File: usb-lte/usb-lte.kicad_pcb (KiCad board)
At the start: 4 copper layers, 26 x 45 mm, 89 parts, among them J1 Sim slot, J2 Conn_Coaxial, J3 Conn_Coaxial, J4 Conn_Coaxial, P1 USB_C_Plug_USB2.0, Q1 MBT3904DW1, Q2 MBT3904DW1, Q3 MBT3904DW1, SW1 B3U-1000P, U1 TPS62A02APDDC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

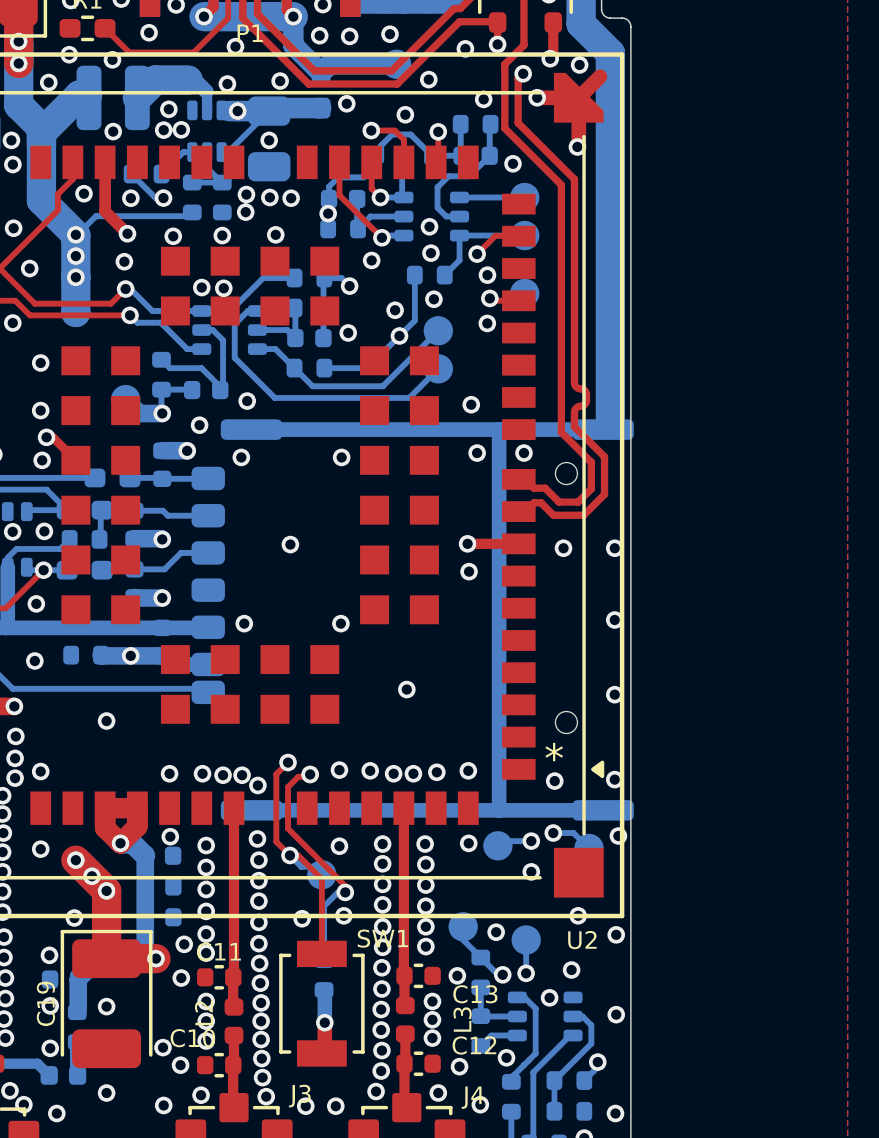
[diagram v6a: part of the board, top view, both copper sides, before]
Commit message: Update test points
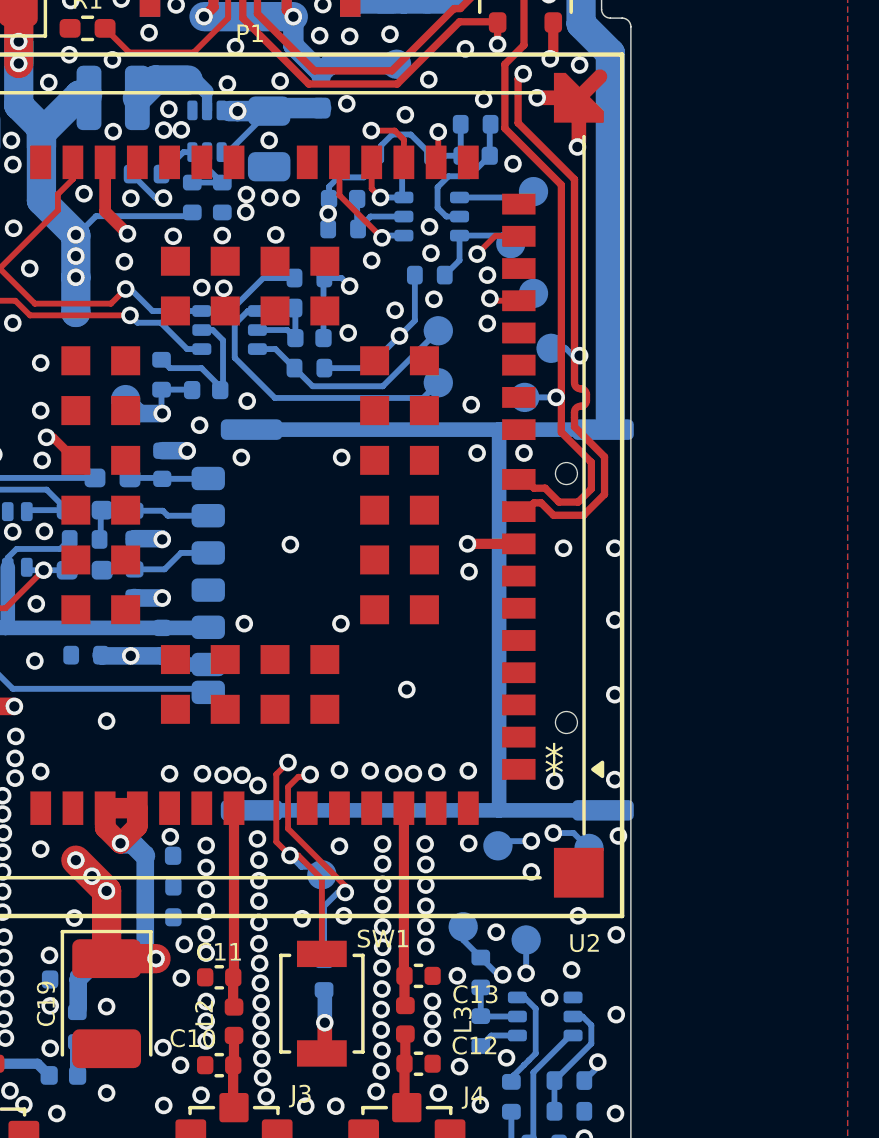
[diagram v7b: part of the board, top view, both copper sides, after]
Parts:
- added TP18: TestPoint, footprints:TestPoint_Pad_1mm, B.Cu at (160.9, 103.7)
- added TP19: TestPoint, footprints:TestPoint_Pad_1mm, B.Cu at (160.0, 105.3)
- R13: value 510k -> 560k
- moved TP10 0.55 mm to (159.5, 100.1)
- moved TP6 0.47 mm to (157.0, 104.8)
- moved TP11 0.36 mm to (160.3, 98.3)
- moved TP7 0.30 mm to (160.3, 101.8)
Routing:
- net USB_DP: track 33.5 -> 34.7 mm, vias 2 -> 3
- net USB_DN: track 34.5 -> 35.8 mm, vias 0 -> 1
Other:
- board text added: "D+"
- board text added: "D-"

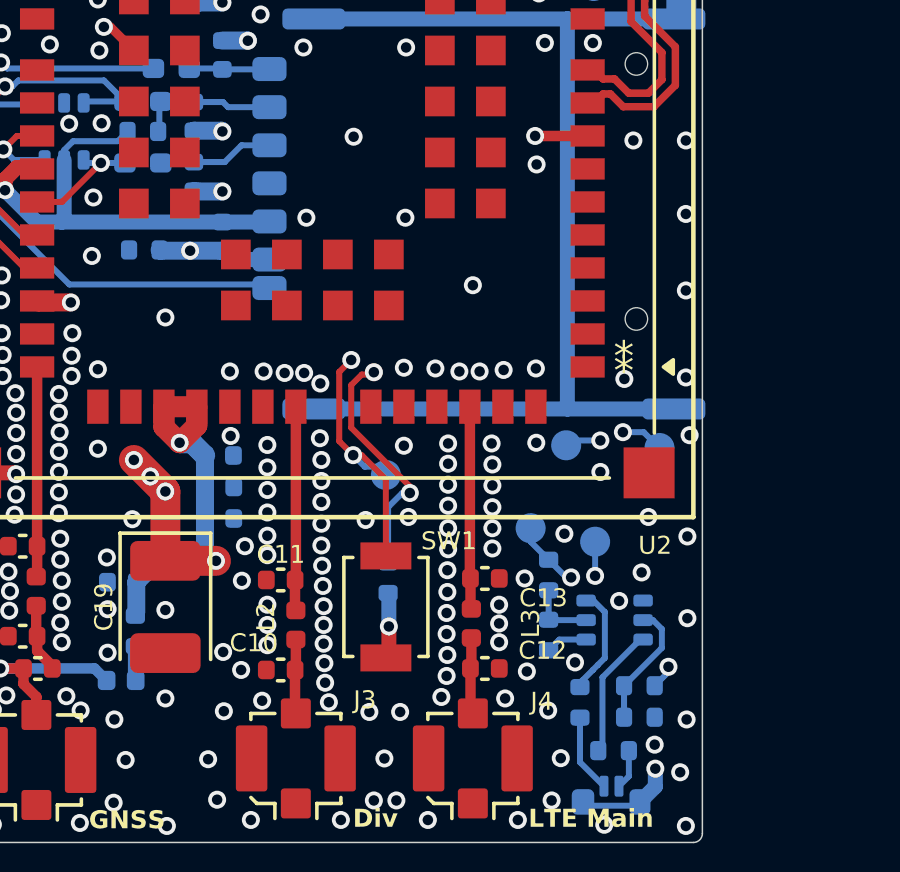
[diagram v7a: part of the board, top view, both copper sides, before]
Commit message: Remove USB boot key, add autostart pull down
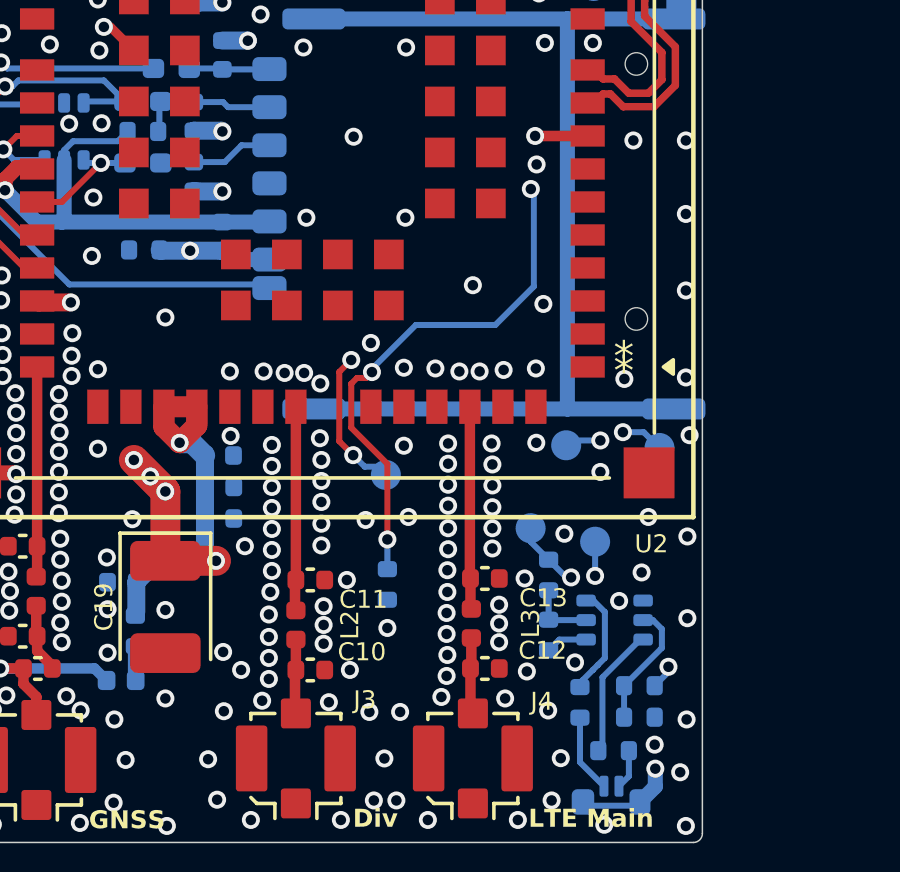
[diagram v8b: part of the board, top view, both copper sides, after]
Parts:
- removed SW1: B3U-1000P, Button_Switch_SMD:SW_SPST_B3U-1000P
- R27: value 4.7k -> 10k
- moved C10 0.99 mm to (150.5, 128.2), turned to 0 degrees
- moved C11 0.99 mm to (150.5, 125.2), turned to 0 degrees
- moved R27 0.23 mm to (153.1, 125.3)
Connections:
- R27 pad 1: Net-(R27-Pad1) -> GND
- R27 pad 2: VDD_EXT -> MODEM_PWRKEY
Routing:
- net VDD_EXT: track 56.0 -> 33.5 mm, vias 6 -> 4
- net MODEM_PWRKEY: track 25.4 -> 42.8 mm, vias 2 -> 5
- net MODEM_USB_BOOT: track 41.4 -> 37.4 mm
- net Net-(R27-Pad1): track 2.22 -> 0.00 mm, vias 1 -> 0
- net GND: vias 268 -> 271
